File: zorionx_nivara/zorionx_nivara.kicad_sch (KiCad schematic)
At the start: 9 parts, among them J1 Screw_Terminal_01x02, J2 Screw_Terminal_01x04, J3 Screw_Terminal_01x04, J4 Screw_Terminal_01x02, J5 Screw_Terminal_01x02, J6 Screw_Terminal_01x03, J7 Screw_Terminal_01x04, J8 Screw_Terminal_01x03, J9 Screw_Terminal_01x06

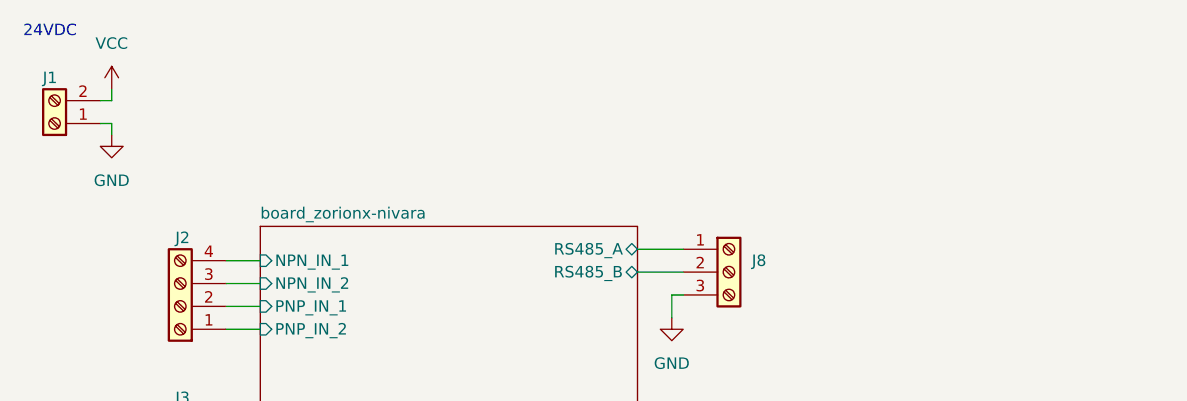
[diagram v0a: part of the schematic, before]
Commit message: ruteo power
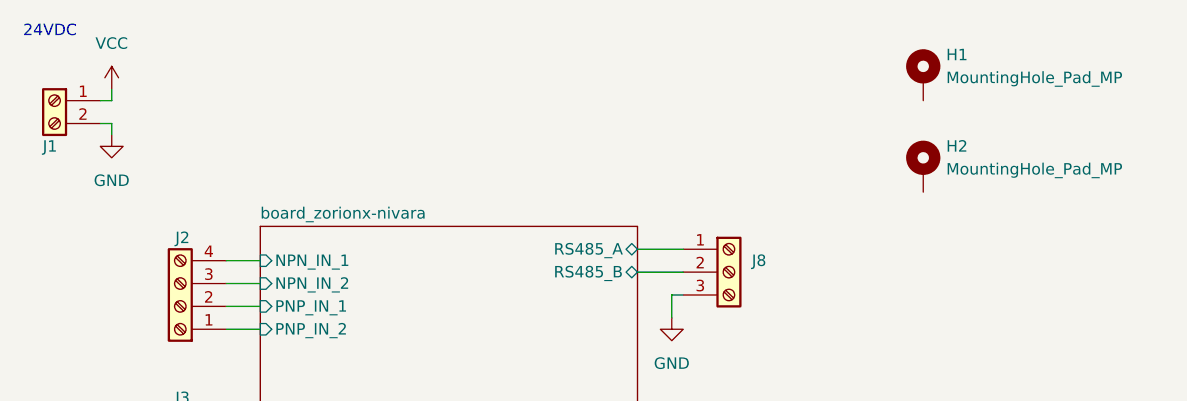
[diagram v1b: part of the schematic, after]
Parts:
- added H1, H2: MountingHole_Pad_MP, MountingHole:MountingHole_3.2mm_M3_DIN965_Pad, symbol Mechanical:MountingHole_Pad_MP
- J1, J4, J5: footprint (none) -> TerminalBlock:TerminalBlock_MaiXu_MX126-5.0-02P_1x02_P5.00mm
- J2, J3, J7: footprint (none) -> TerminalBlock:TerminalBlock_MaiXu_MX126-5.0-04P_1x04_P5.00mm
- J6, J8: footprint (none) -> TerminalBlock:TerminalBlock_MaiXu_MX126-5.0-03P_1x03_P5.00mm
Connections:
- net GND: now also J1.2 (Pin_2); no longer J1.1 (Pin_1)
- net VCC: now also J1.1 (Pin_1); no longer J1.2 (Pin_2)
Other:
- moved on the sheet: J1
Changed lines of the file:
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@@
+	(wire
+		(pts
+			(xy 123.19 73.66) (xy 124.46 73.66)
+		)
+		(stroke
+			(width 0)
+			(type default)
+		)
+	)
 	(wire
 		(pts
@@
 		(pts
 			(xy 137.16 111.76) (xy 140.97 111.76)
-		)
-		(stroke
-			(width 0)
-			(type default)
-		)
-	)
-	(wire
-		(pts
-			(xy 123.19 73.66) (xy 124.46 73.66)
 		)
 		(stroke
@@
 			)
 		)
-		(property "Footprint" ""
+		(property "Footprint" "TerminalBlock:TerminalBlock_MaiXu_MX126-5.0-04P_1x04_P5.00mm"
 			(at 191.77 124.46 0)
 			(effects
@@
 			)
 		)
-		(property "Footprint" ""
+		(property "Footprint" "TerminalBlock:TerminalBlock_MaiXu_MX126-5.0-02P_1x02_P5.00mm"
 			(at 132.08 130.81 0)
 			(effects
@@
 			)
 		)
-		(property "Footprint" ""
+		(property "Footprint" "TerminalBlock:TerminalBlock_MaiXu_MX126-5.0-04P_1x04_P5.00mm"
 			(at 132.08 111.76 0)
 			(effects
@@
 	(symbol
 		(lib_id "Connector:Screw_Terminal_01x02")
-		(at 118.11 73.66 180)
+		(at 118.11 71.12 0)
+		(mirror y)
 		(unit 1)
 		(exclude_from_sim no)
@@
 		(dnp no)
 		(property "Reference" "J1"
-			(at 117.602 68.58 0)
+			(at 117.602 76.2 0)
 			(effects
 				(font
@@
 		)
 		(property "Value" "Screw_Terminal_01x02"
-			(at 118.11 67.31 0)
-			(effects
-				(font
-					(size 1.27 1.27)
-				)
-				(hide yes)
-			)
-		)
-		(property "Footprint" ""
-			(at 118.11 73.66 0)
+			(at 118.11 77.47 0)
+			(effects
+				(font
+					(size 1.27 1.27)
+				)
+				(hide yes)
+			)
+		)
+		(property "Footprint" "TerminalBlock:TerminalBlock_MaiXu_MX126-5.0-02P_1x02_P5.00mm"
+			(at 118.11 71.12 0)
 			(effects
 				(font
@@
 		)
 		(property "Datasheet" "~"
-			(at 118.11 73.66 0)
+			(at 118.11 71.12 0)
 			(effects
 				(font
@@
 		)
 		(property "Description" "Generic screw terminal, single row, 01x02, script generated (kicad-library-utils/schlib/autogen/connector/)"
-			(at 118.11 73.66 0)
+			(at 118.11 71.12 0)
 			(effects
 				(font
@@
 			)
 		)
-		(property "Footprint" ""
+		(property "Footprint" "TerminalBlock:TerminalBlock_MaiXu_MX126-5.0-03P_1x03_P5.00mm"
 			(at 193.04 90.17 0)
 			(effects
@@
 			)
 		)
-		(property "Footprint" ""
+		(property "Footprint" "TerminalBlock:TerminalBlock_MaiXu_MX126-5.0-03P_1x03_P5.00mm"
 			(at 191.77 109.22 0)
 			(effects
@@
 			)
 		)
-		(property "Footprint" ""
+		(property "Footprint" "TerminalBlock:TerminalBlock_MaiXu_MX126-5.0-04P_1x04_P5.00mm"
 			(at 132.08 93.98 0)
 			(effects
@@
 			)
 		)
-		(property "Footprint" ""
+		(property "Footprint" "TerminalBlock:TerminalBlock_MaiXu_MX126-5.0-02P_1x02_P5.00mm"
 			(at 132.08 154.94 0)
 			(effects
@@
 				(path "/f2de36b2-81cb-4123-9a7d-6a58bb468c83"
 					(reference "J5")
+					(unit 1)
+				)
+			)
+		)
+	)
+	(symbol
+		(lib_id "Mechanical:MountingHole_Pad_MP")
+		(at 214.63 78.74 0)
+		(unit 1)
+		(exclude_from_sim no)
+		(in_bom no)
+		(on_board yes)
+		(dnp no)
+		(fields_autoplaced yes)
+		(property "Reference" "H2"
+			(at 217.17 76.1999 0)
+			(effects
+				(font
+					(size 1.27 1.27)
+				)
+				(justify left)
+			)
+		)
+		(property "Value" "MountingHole_Pad_MP"
+			(at 217.17 78.7399 0)
+			(effects
+				(font
+					(size 1.27 1.27)
+				)
+				(justify left)
+			)
+		)
+		(property "Footprint" "MountingHole:MountingHole_3.2mm_M3_DIN965_Pad"
+			(at 214.63 78.74 0)
+			(effects
+				(font
+					(size 1.27 1.27)
+				)
+				(hide yes)
+			)
+		)
+		(property "Datasheet" "~"
+			(at 214.63 78.74 0)
+			(effects
+				(font
+					(size 1.27 1.27)
+				)
+				(hide yes)
+			)
+		)
+		(property "Description" "Mounting Hole with connection as pad named MP"
+			(at 214.63 78.74 0)
+			(effects
+				(font
+					(size 1.27 1.27)
+				)
+				(hide yes)
+			)
+		)
+		(pin "MP"
+		)
+		(instances
+			(project "zorionx_nivara"
+				(path "/f2de36b2-81cb-4123-9a7d-6a58bb468c83"
+					(reference "H2")
 					(unit 1)
 				)
@@
 					(unit 1)
 				)
+			)
+		)
+	)
+	(symbol
+		(lib_id "Mechanical:MountingHole_Pad_MP")
+		(at 214.63 68.58 0)
+		(unit 1)
+		(exclude_from_sim no)
+		(in_bom no)
+		(on_board yes)
+		(dnp no)
+		(fields_autoplaced yes)
+		(property "Reference" "H1"
+			(at 217.17 66.0399 0)
+			(effects
+				(font
+					(size 1.27 1.27)
+				)
+				(justify left)
+			)
+		)
+		(property "Value" "MountingHole_Pad_MP"
+			(at 217.17 68.5799 0)
+			(effects
+				(font
+					(size 1.27 1.27)
+				)
+				(justify left)
+			)
+		)
+		(property "Footprint" "MountingHole:MountingHole_3.2mm_M3_DIN965_Pad"
+			(at 214.63 68.58 0)
+			(effects
+				(font
+					(size 1.27 1.27)
+				)
+				(hide yes)
+			)
+		)
+		(property "Datasheet" "~"
+			(at 214.63 68.58 0)
+			(effects
+				(font
+					(size 1.27 1.27)
+				)
+				(hide yes)
+			)
+		)
+		(property "Description" "Mounting Hole with connection as pad named MP"
+			(at 214.63 68.58 0)
+			(effects
+				(font
+					(size 1.27 1.27)
+				)
+				(hide yes)
+			)
+		)
+		(pin "MP"
+		)
+		(instances
+			(project ""
+				(path "/f2de36b2-81cb-4123-9a7d-6a58bb468c83"
+					(reference "H1")
+					(unit 1)
+				)
